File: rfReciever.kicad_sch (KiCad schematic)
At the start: 31 parts, among them P2 USB_C_Plug_USB2.0, SW1 RF_RESET, U1 CP2102N-Axx-xQFN20, U4 USBLC6-2SC6, X1 DigiXBeeRX900Micro

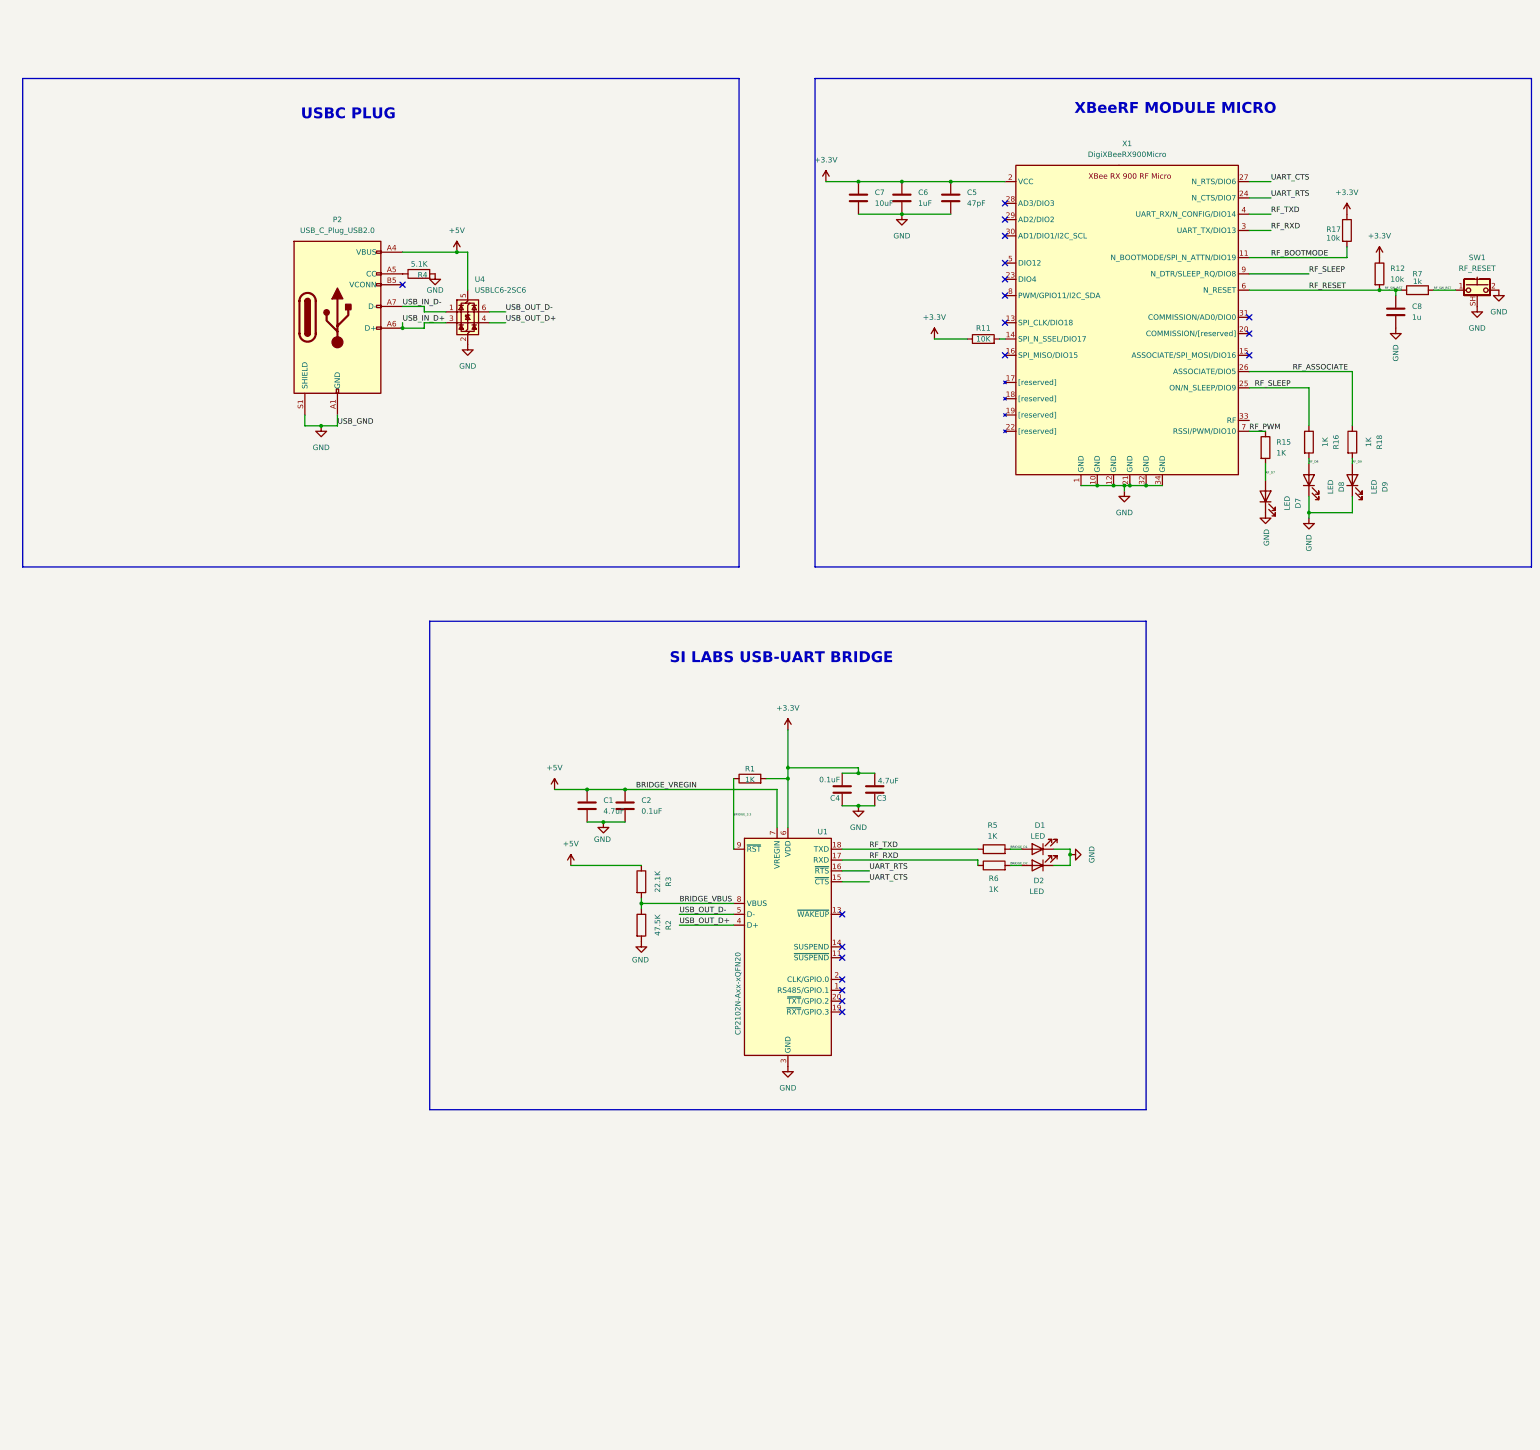
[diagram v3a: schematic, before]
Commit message: Reworked schematic, partial layout
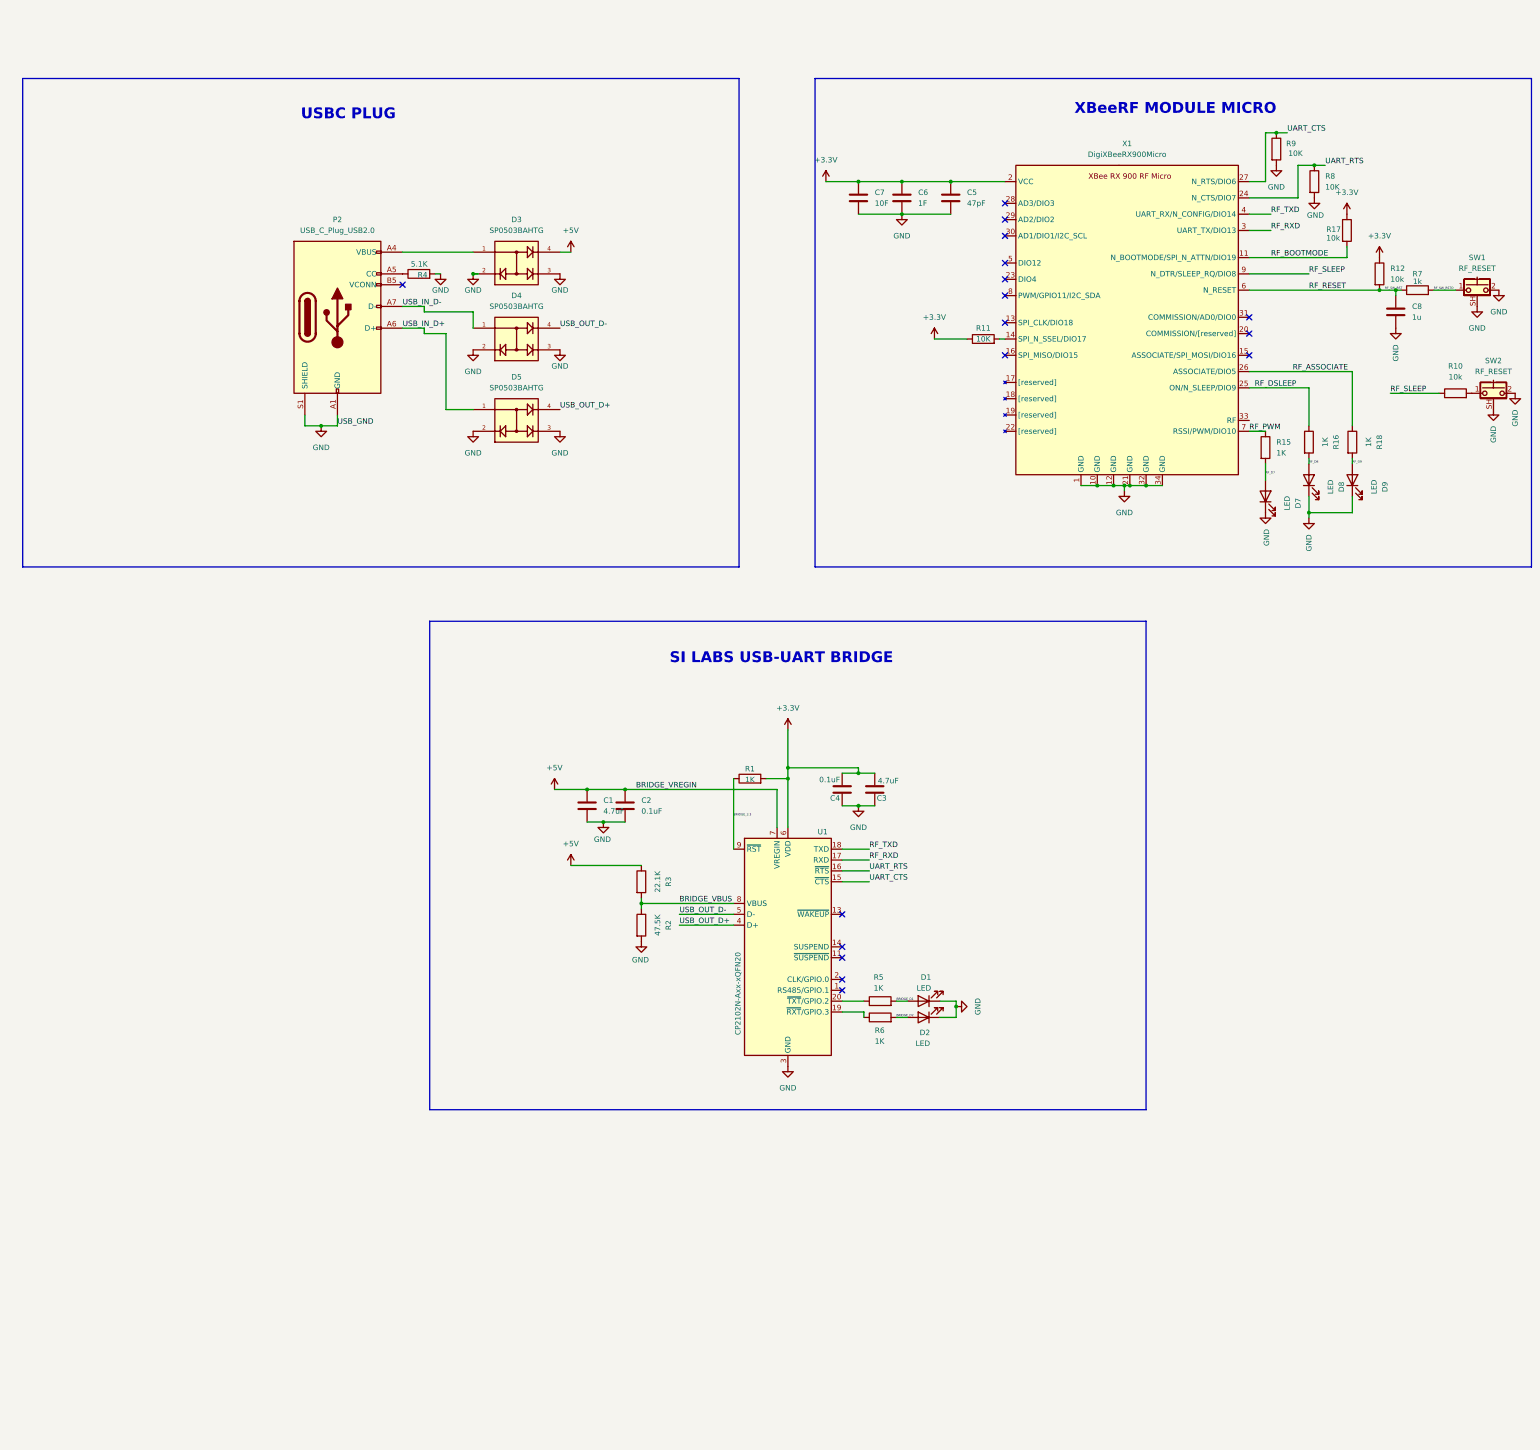
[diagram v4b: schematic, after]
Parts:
- removed U4: USBLC6-2SC6, Package_TO_SOT_SMD:SOT-23-6, symbol Power_Protection:USBLC6-2SC6
- added D3, D4, D5: SP0503BAHTG, rfReciever-Footprints:SOT143, symbol 5vESD:SP0503BAHTG
- added R10: 10k, Resistor_SMD:R_0805_2012Metric, symbol Device:R
- added R8, R9: 10K, Resistor_SMD:R_0805_2012Metric, symbol Device:R
- added SW2: RF_RESET, Button_Switch_SMD:SW_SPST_CK_KMS2xxGP, symbol Switch:CK_KMS2xxG
- C6: value 1uF -> 1F
- C7: value 10uF -> 10F
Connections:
- net +5V: now also D3.4; no longer P2.A4 (VBUS), P2.A9 (VBUS), P2.B4 (VBUS), P2.B9 (VBUS)
- net GND: now also D3.2, D3.3, D4.2, D4.3, D5.2, D5.3, R8.2, R9.2, SW2.2, SW2.SH (B)
- net RF_RESET: no longer R7.2, SW1.1
- net RF_RXD: no longer R6.1
- net RF_SLEEP: now also R10.1; no longer R16.1, X1.25 (ON/N_SLEEP/DIO9)
- net RF_TXD: no longer R5.1
- net UART_CTS: now also R9.1
- net UART_RTS: now also R8.1
- net USB_IN_D+: now also D5.1
- net USB_IN_D-: now also D4.1
- net USB_OUT_D+: now also D5.4
- net USB_OUT_D-: now also D4.4
- net at U1.19 (~{RXT}/GPIO.3): now also R6.1
- net at U1.20 (~{TXT}/GPIO.2): now also R5.1
- new net: R10.2, SW2.1
- new net: D3.1, P2.A4 (VBUS), P2.A9 (VBUS), P2.B4 (VBUS), P2.B9 (VBUS)
- new net RF_DSLEEP: R16.1, X1.25 (ON/N_SLEEP/DIO9)
- new net RF_SW_RSTO: R7.2, SW1.1
- no-connect marks 19 -> 17
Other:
- moved on the sheet: D1, D2, R5, R6

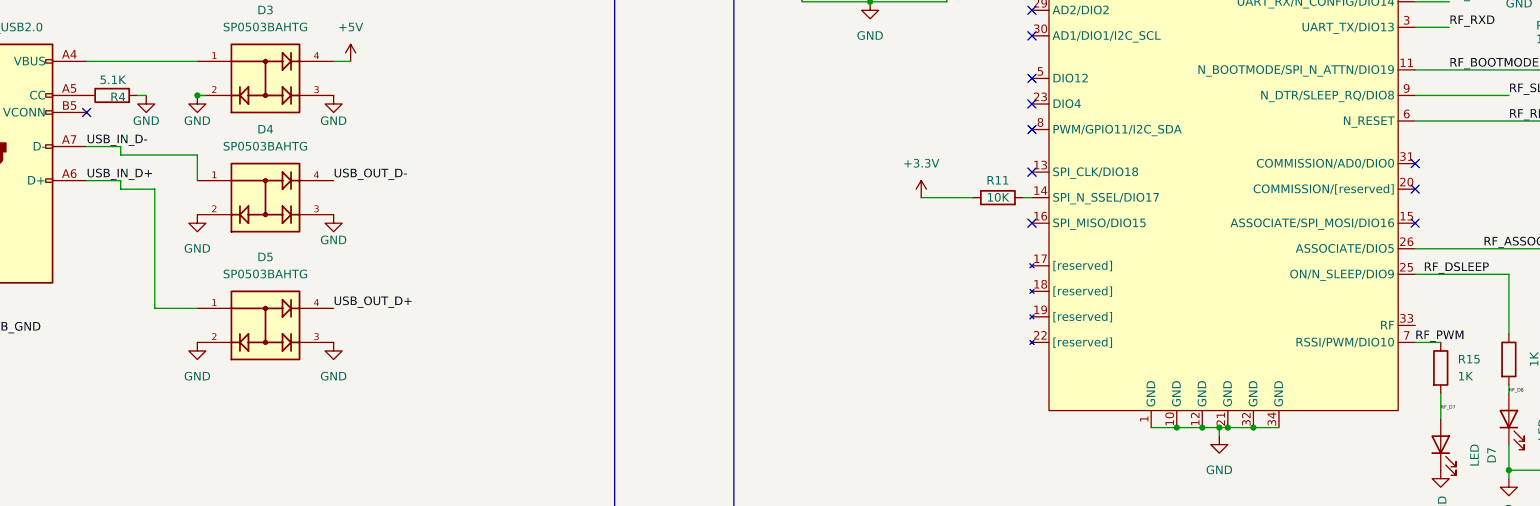
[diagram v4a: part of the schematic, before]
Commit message: 4 layer layout, new esd protection for USB
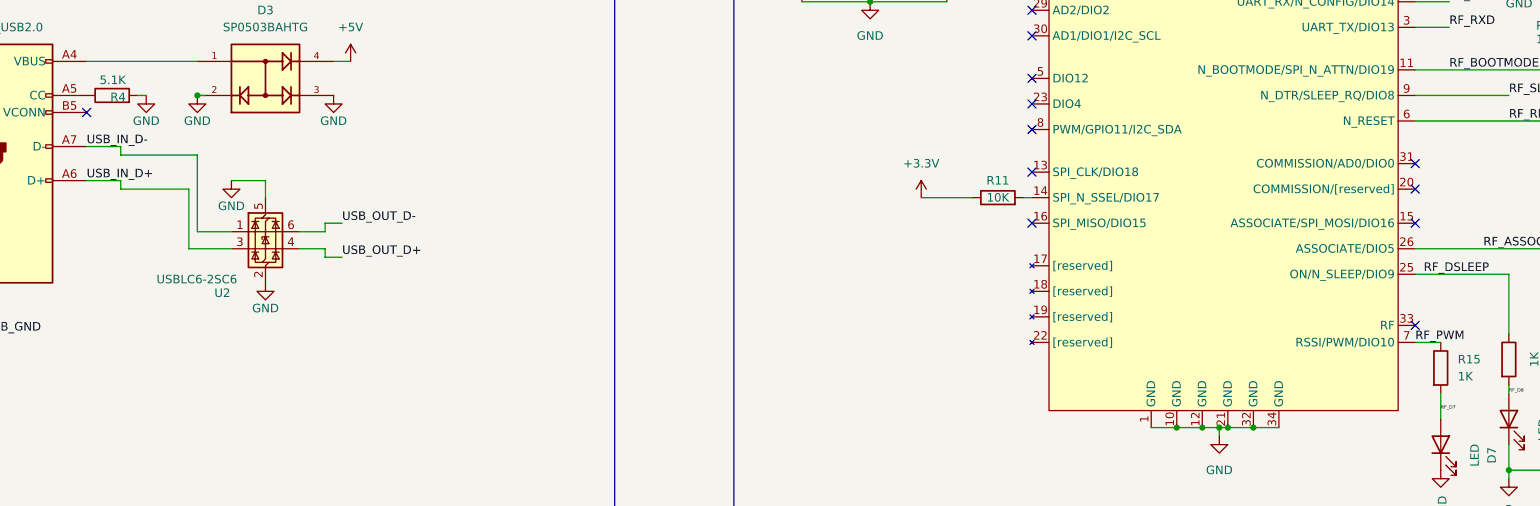
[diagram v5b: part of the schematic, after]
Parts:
- removed D4, D5: SP0503BAHTG, rfReciever-Footprints:SOT143, symbol 5vESD:SP0503BAHTG
- added U2: USBLC6-2SC6, Package_TO_SOT_SMD:SOT-23-6, symbol Power_Protection:USBLC6-2SC6
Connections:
- net GND: now also U2.2 (GND), U2.5 (VBUS)
- net USB_IN_D+: now also U2.3 (I/O2)
- net USB_IN_D-: now also U2.1 (I/O1)
- net USB_OUT_D+: now also U2.4 (I/O2)
- net USB_OUT_D-: now also U2.6 (I/O1)
- no-connect marks 17 -> 18

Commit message: Fixed up layout + shematic
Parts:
- added C9: 1u, Capacitor_SMD:C_0805_2012Metric, symbol Device:C
- added R13: 1k, Resistor_SMD:R_0805_2012Metric, symbol Device:R
- SW2: value RF_RESET -> RF_SLEEP
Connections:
- net +3.3V: now also R10.2
- net +5V: now also D3.1, P2.A4 (VBUS), P2.A9 (VBUS), P2.B4 (VBUS), P2.B9 (VBUS)
- net GND: now also C9.2
- net RF_SLEEP: now also C9.1, R13.1
- net RF_SW_SLEEP: now reaches SW2.1
- net RF_SW_SLEEP: now also R13.2; no longer R10.2
- net RF_SW_RSTO renamed RF_SW_RESET
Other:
- moved on the sheet: R10, SW2

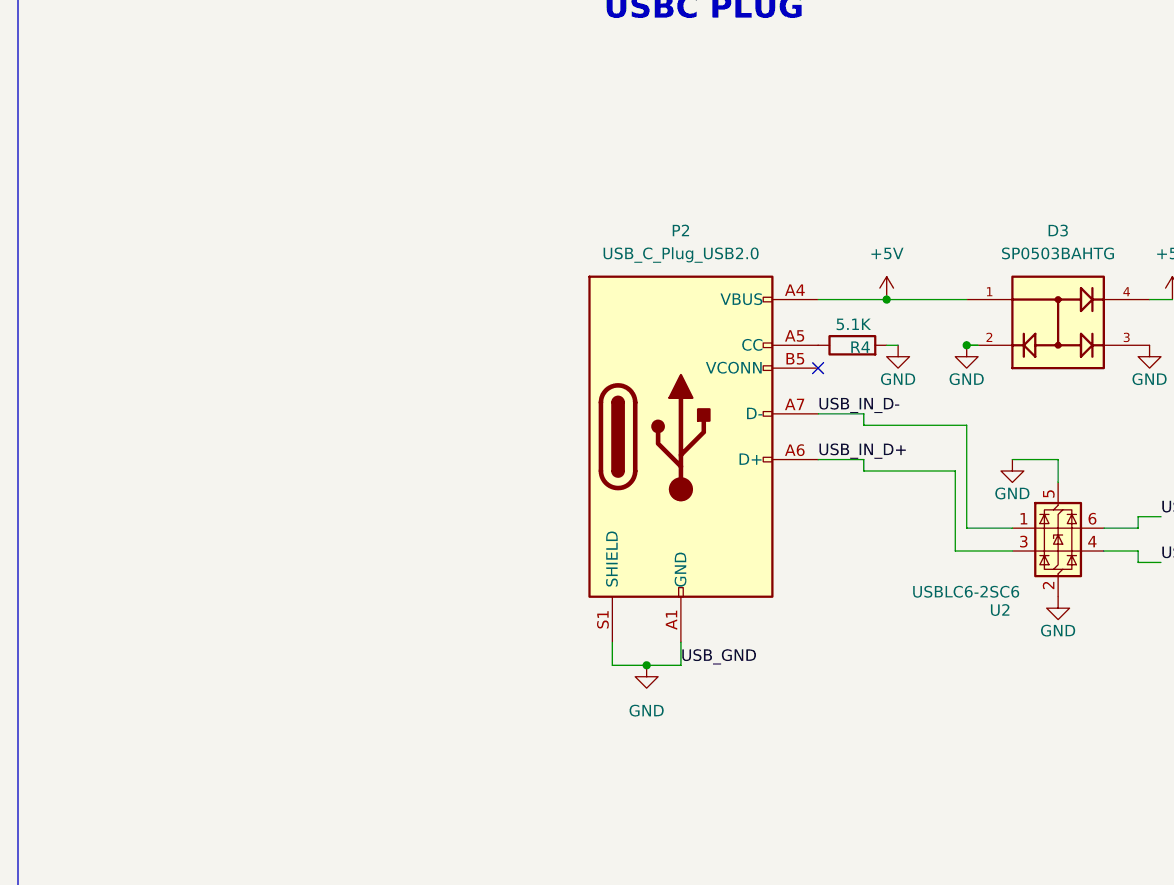
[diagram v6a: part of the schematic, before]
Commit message: new molex connector, final layout
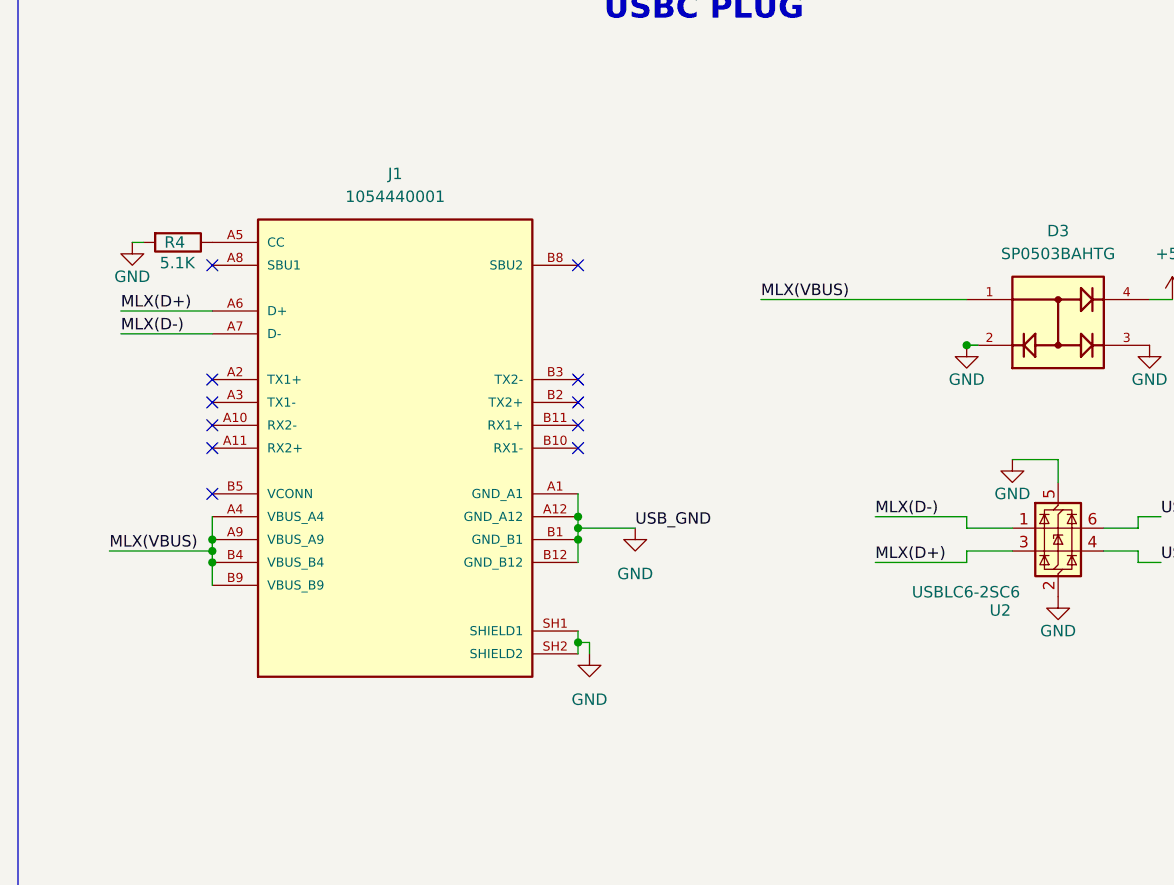
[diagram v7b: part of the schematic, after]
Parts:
- removed P2: USB_C_Plug_USB2.0, Connector_USB:USB_C_Plug_JAE_DX07P024AJ1, symbol Connector:USB_C_Plug_USB2.0
- added J1: 1054440001, rfReciever-Footprints:MOLEX_1054440001, symbol Molex USBC:1054440001
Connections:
- net +5V: no longer D3.1
- net GND: now also J1.A1 (GND_A1), J1.A12 (GND_A12), J1.B1 (GND_B1), J1.B12 (GND_B12), J1.SH1 (SHIELD1), J1.SH2 (SHIELD2)
- net at R4.1: now also J1.A5 (CC)
- net USB_IN_D+ renamed MLX(D+)
- net MLX(D+): now also J1.A6 (D+)
- net USB_IN_D- renamed MLX(D-)
- net MLX(D-): now also J1.A7 (D-)
- new net MLX(VBUS): D3.1, J1.A4 (VBUS_A4), J1.A9 (VBUS_A9), J1.B4 (VBUS_B4), J1.B9 (VBUS_B9)
- no-connect marks 18 -> 28
